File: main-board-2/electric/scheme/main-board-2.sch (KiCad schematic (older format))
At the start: 71 parts

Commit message: Made scheme for main-board-2.
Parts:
- removed P?: PWR-IN, symbol CONN_2
- removed R? (x3): 100, symbol R
- removed U?: L293, symbol L293
- removed U? (x2): LM317, ~, symbol LM317
- added C15, C16, C17: 100n, symbol C
- added D10, D3, D4, D5, D6, D7, D8, D9: 1n5819, ~, symbol DIODESCH
- added K3: power-switch, symbol CONN_3
- added Q1, Q9: IRLML2244, symbol MOS_P
- added Q11: sot223, symbol MOS_P
- added Q2, Q7: BC847, symbol NPN
- added R10, R25, R8: 30k, symbol R
- added R23, R9: 1k, symbol R
- added U1, U2: LM317AT, TO-220, symbol LM317AT
- added U3: L298, symbol L298
- C1: renamed from C?; value CP1 -> 1000u
- C14: renamed from C?; value 10u -> 4u7
- C5: renamed from C?; value CP1 -> 54u
- K4: renamed from K?; value CONN_3 -> usb-power-switch
- R13: renamed from R?; value 10k -> 30k
- R19, R20, R24: renamed from R?; value 500 -> 1k
- gave numbers to parts that had none: 56
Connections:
- net labels added: addon-trigger, rpi-pwr-en, trigger-button, usb-power
- net labels removed: +6V, batt-volt, boost-current, boost-pwm, buck-current, buck-out-5v, buck-pwm, buck-volt, just-power-source, light, solar, solar+, solar-volt, temperature, wakeup
- wire segments 265 -> 298
- no-connect marks 11 -> 18
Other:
- note added: "If jumper is here \nUSB is a voltage \ninput."
- note added: "If jumper is here \nUSB is a voltage \noutput."
- note added: "No I2C pullups here as \nthere are on raspberry-pi."
- note added: "RPi power."
- note added: "This one is optional \nfor high voltages >20V."
- note removed: "Jumper here tells MCU to never turn 5V \nconverter off."
- note removed: "No pullups here as there are on raspberry-pi."
- note removed: "Optionally could be USB powered \nthrough "solar+". It is because of \nability to control current through \n"solar+"."
- note removed: "Power source such as solar panel.\nIt's voltage shouldn't be greater then \nbattery's voltage. It is because \nbattery is changed using boost \nscheme."
- moved on the sheet: C5, C6, K4, P10, P11, P2, P6, P7, P8, P9, Q10, Q3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

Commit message: s
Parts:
- C1: value 1000u -> 54u
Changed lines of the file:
@@
 P 1300 2000
 F 0 "C1" H 1350 2100 50  0000 L CNN
-F 1 "1000u" H 1350 1900 50  0000 L CNN
+F 1 "54u" H 1350 1900 50  0000 L CNN
 F 2 "~" H 1300 2000 60  0000 C CNN
 F 3 "~" H 1300 2000 60  0000 C CNN

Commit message: a
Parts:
- removed C17: 100n, symbol C
- removed K1: CONN_3, symbol CONN_3
- removed K2: flashing, symbol CONN_3
- added D11, D12, D13, D14: DIODE, ~, symbol DIODE
- added P12, P13: TST, ~, symbol TST
- added P14: rst, ~, symbol TST
- added P15: gpio-big, symbol CONN_12X2
- added P16: gpio-small, symbol CONN_3X2
- added Q12: bc857, ~, symbol PNP
- added Q13: irlml2244, ~, symbol MOSFET_P
- added R31, R32, R33, R34: 30k, symbol R
- added R35, R36, R37, R38: 0.1, ~, symbol R
- added R39, R41, R44, R46, R51, R52: 30k, ~, symbol R
- added R40, R42, R43, R45, R47, R48: 1k, ~, symbol R
- added R49, R50: 9, ~, symbol R
- added U5, U6: LM317AEMP, SOT-223, symbol LM317AEMP
- added U7: LM293, symbol LM293
- added W1: sc-rpi-5v, symbol TEST
- added W10: sc-moto-4, symbol TEST
- added W11: sc-moto-2, symbol TEST
- added W12, W4, W5: TEST, symbol TEST
- added W2: sc-addon-5v, symbol TEST
- added W3: sc-addon-3.3, symbol TEST
- added W6: sc-sense-2, symbol TEST
- added W7: sc-sense-1, symbol TEST
- added W8: sc-moto-3, symbol TEST
- added W9: sc-moto-1, symbol TEST
- P1: value PWR-IN -> batt
- P10: value TST -> screw-2
- P7: value TST -> screw-3
- P8: value TST -> screw-1
- P9: value TST -> screw-4
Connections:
- net labels added: cur-sense-1, cur-sense-2, gnd, gpio-1, gpio-2, gpio-3, gpio-4, gpio-5, gpio-6, gpio-7, gpio-8, gpio-9, in-moto1, in-moto2, in-moto3, in-moto4
- net labels removed: adon-vdd
- wire segments 298 -> 439
- no-connect marks 18 -> 9
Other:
- note added: "Again either a couple of short \ncircuit wires or on/off circuit."
- note added: "Current limiting to 400mA when USB is \nused for powering the board."
- note added: "Current sense\n0.1Ohm x 2units \nare 0.05Ohm.\nAt 2Amps it would be \nP=2^2*0.05 = 0.2W.\n0.1W per one R unit.\nAnd it is <0.125W."
- note added: "Either on/off circuit or \nshourt-circuit wire."
- note added: "Here again either short \ncircuit wires or circuits for \ncurrent limiting."
- note added: "Install either TO-220 or SO-223"
- note added: "This one isn't actually needed for current limiting.\nBut when powered from battery with voltage >12V \nGS voltage shouldn't be greater then 12V. This \nresistor makes it 1/2 of batt+ value."
- note removed: "Programming socket"
- note removed: "Serial socket"
- moved on the sheet: C15, C16, K4, Q11, Q7, Q9, R23, R25, R27, R28, R29, R30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

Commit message: Optimizing board...
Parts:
- removed D11, D12, D13, D14: DIODE, ~, symbol DIODE
- removed P11: moto, symbol CONN_4
- removed R44, R46: 30k, ~, symbol R
- removed R47, R48: 1k, ~, symbol R
- removed W10: sc-moto-4, symbol TEST
- removed W11: sc-moto-2, symbol TEST
- added P16: moto-1, symbol CONN_2
- added P17: moto-2, symbol CONN_2
- W8: value sc-moto-3 -> sc-moto-2
- renumbered K3 to K1, K4 to K2, P7 to P10, P8 to P11, P9 to P12, P10 to P13, P15 to P14, P16 to P15, P12 to P5, P13 to P6, P5 to P7, P6 to P8, P14 to P9, R31 to R17, R32 to R18, R17 to R19, R18 to R20, R19 to R21, R20 to R22, R21 to R23, R22 to R24, R23 to R25, R24 to R26, R25 to R27, R33 to R28, R26 to R29, R34 to R30, R27 to R31, R28 to R32, R29 to R33, R30 to R34, R45 to R44, R49 to R45, R50 to R46, R51 to R47, R52 to R48, U5 to U1, U1 to U2, U6 to U3, U2 to U4, U7 to U5, U3 to U6, U4 to U7, W12 to W10
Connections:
- net labels added: moto-en-1, moto-en-2
- net labels removed: moto1, moto2, moto3, moto4
- wire segments 439 -> 421
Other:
- note added: "This comparator has open collector \noutput type. So it matters only when \nlevel goes low."

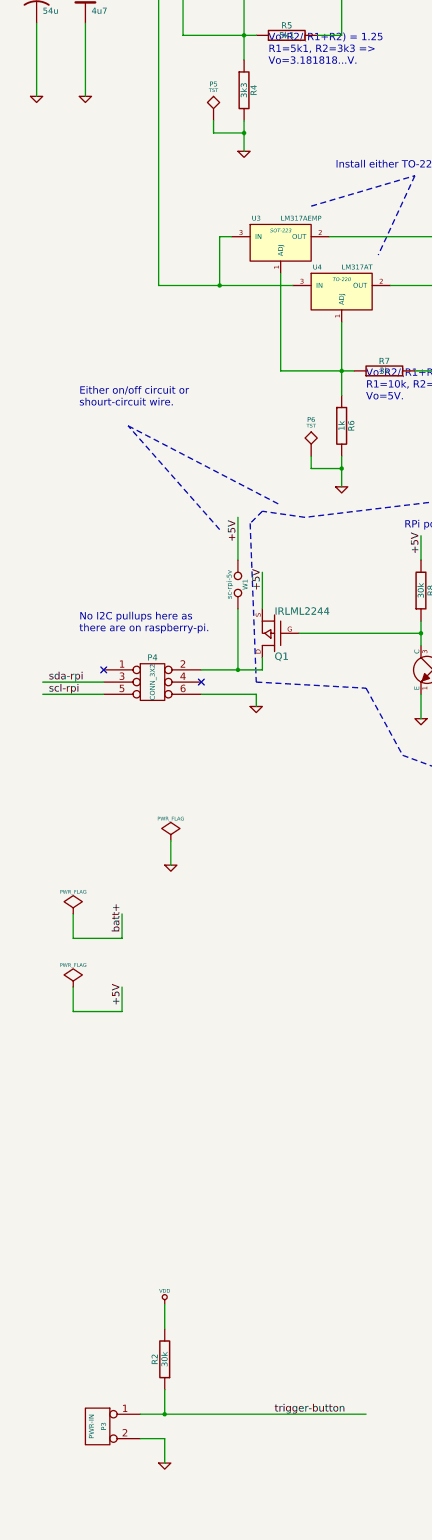
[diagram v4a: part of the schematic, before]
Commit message: Assigned components to footprints.
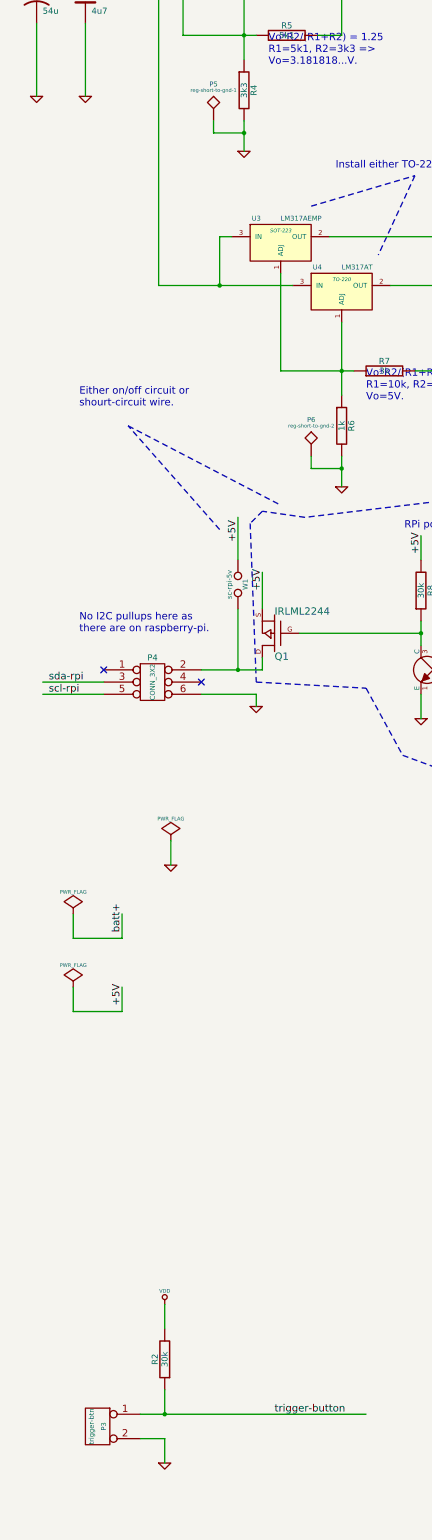
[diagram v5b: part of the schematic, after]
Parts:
- P3: value PWR-IN -> trigger-btn
- P5: value TST -> reg-short-to-gnd-1
- P6: value TST -> reg-short-to-gnd-2
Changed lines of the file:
@@
 P 1800 13700
 F 0 "P3" V 1750 13700 40  0000 C CNN
-F 1 "PWR-IN" V 1850 13700 40  0000 C CNN
+F 1 "trigger-btn" V 1850 13700 40  0000 C CNN
 F 2 "" H 1800 13700 60  0001 C CNN
 F 3 "" H 1800 13700 60  0001 C CNN
@@
 P 2750 3000
 F 0 "P5" H 2750 3300 40  0000 C CNN
-F 1 "TST" H 2750 3250 30  0000 C CNN
+F 1 "reg-short-to-gnd-1" H 2750 3250 30  0000 C CNN
 F 2 "~" H 2750 3000 60  0000 C CNN
 F 3 "~" H 2750 3000 60  0000 C CNN
@@
 P 3550 5750
 F 0 "P6" H 3550 6050 40  0000 C CNN
-F 1 "TST" H 3550 6000 30  0000 C CNN
+F 1 "reg-short-to-gnd-2" H 3550 6000 30  0000 C CNN
 F 2 "~" H 3550 5750 60  0000 C CNN
 F 3 "~" H 3550 5750 60  0000 C CNN
